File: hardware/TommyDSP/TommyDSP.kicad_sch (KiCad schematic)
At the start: 7 parts

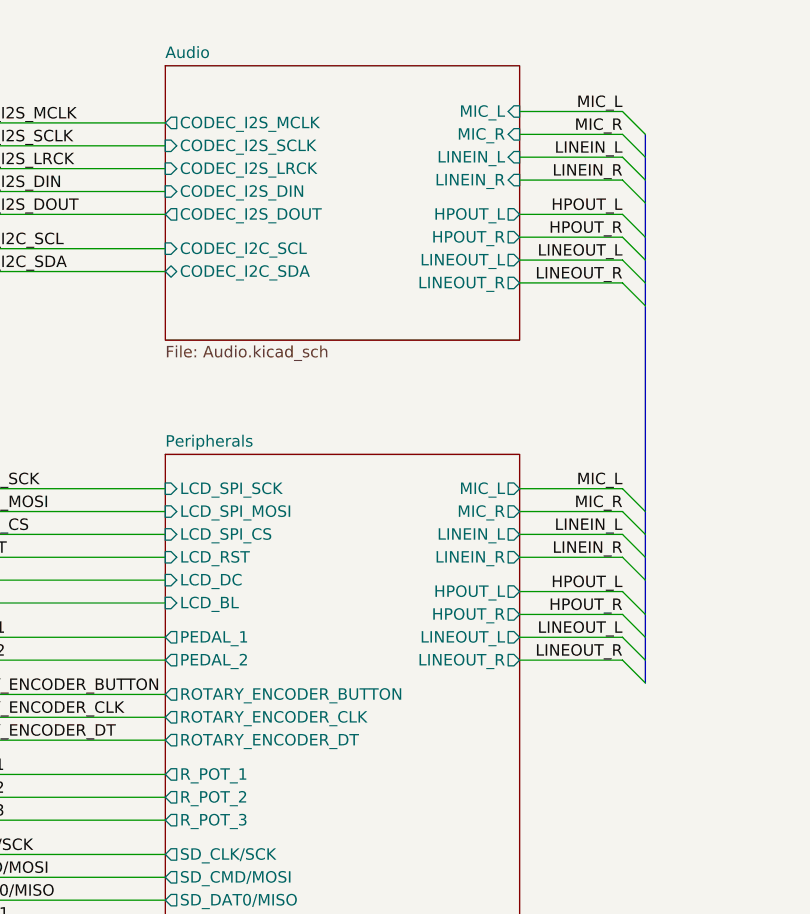
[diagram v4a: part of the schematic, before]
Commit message: hardware: add compatibility for WM8988 CODEC
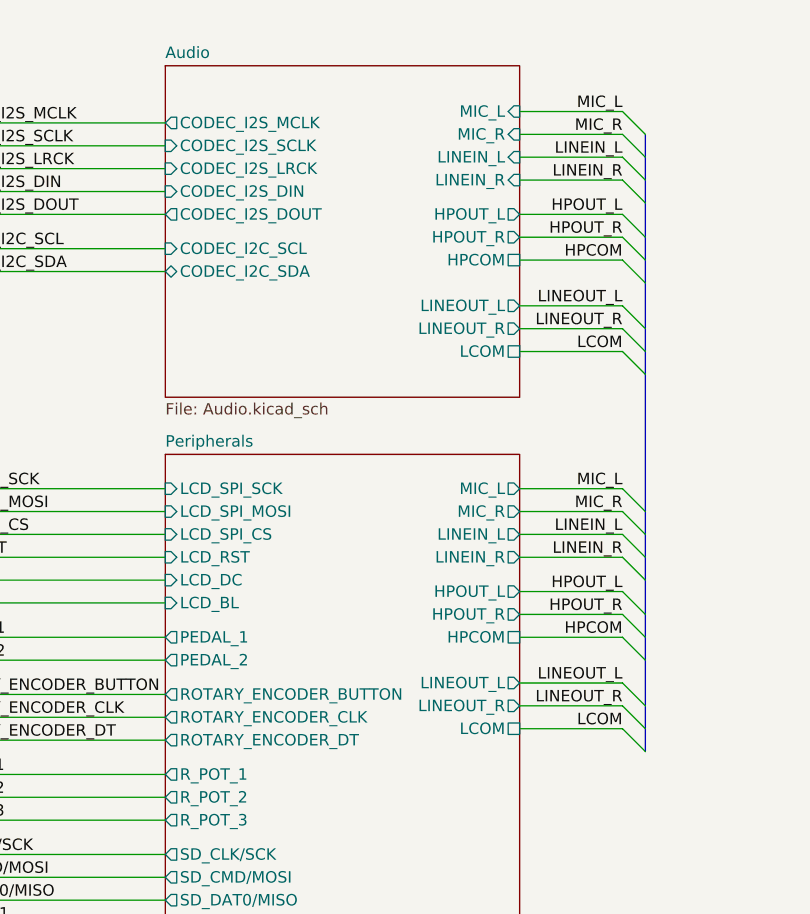
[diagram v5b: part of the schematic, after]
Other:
- sheet Audio ports: added HPCOM, LCOM; removed none
- sheet Peripherals ports: added HPCOM, LCOM; removed none
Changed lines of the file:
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@@
 	)
 	(bus_entry
-		(at 190.5 44.45)
+		(at 190.5 49.53)
 		(size 2.54 2.54)
 		(stroke
@@
 	)
 	(bus_entry
+		(at 190.5 83.82)
+		(size 2.54 2.54)
+		(stroke
+			(width 0)
+			(type default)
+		)
+	)
+	(bus_entry
 		(at 190.5 81.28)
 		(size 2.54 2.54)
@@
 	)
 	(bus_entry
+		(at 190.5 41.91)
+		(size 2.54 2.54)
+		(stroke
+			(width 0)
+			(type default)
+		)
+	)
+	(bus_entry
 		(at 190.5 69.85)
 		(size 2.54 2.54)
@@
 	)
 	(bus_entry
-		(at 190.5 41.91)
+		(at 190.5 93.98)
+		(size 2.54 2.54)
+		(stroke
+			(width 0)
+			(type default)
+		)
+	)
+	(bus_entry
+		(at 190.5 46.99)
 		(size 2.54 2.54)
 		(stroke
@@
 	)
 	(bus_entry
-		(at 190.5 83.82)
+		(at 190.5 88.9)
+		(size 2.54 2.54)
+		(stroke
+			(width 0)
+			(type default)
+		)
+	)
+	(bus_entry
+		(at 190.5 91.44)
 		(size 2.54 2.54)
 		(stroke
@@
 	)
 	(bus_entry
-		(at 190.5 86.36)
+		(at 190.5 52.07)
 		(size 2.54 2.54)
 		(stroke
@@
 		)
 	)
+	(bus
+		(pts
+			(xy 193.04 86.36) (xy 193.04 91.44)
+		)
+		(stroke
+			(width 0)
+			(type default)
+		)
+	)
 	(wire
 		(pts
@@
 	(wire
 		(pts
+			(xy 179.07 52.07) (xy 190.5 52.07)
+		)
+		(stroke
+			(width 0)
+			(type default)
+		)
+	)
+	(wire
+		(pts
 			(xy 114.3 115.57) (xy 139.7 115.57)
 		)
@@
 	(bus
 		(pts
-			(xy 193.04 44.45) (xy 193.04 46.99)
+			(xy 193.04 49.53) (xy 193.04 52.07)
 		)
 		(stroke
@@
 	(wire
 		(pts
+			(xy 179.07 41.91) (xy 190.5 41.91)
+		)
+		(stroke
+			(width 0)
+			(type default)
+		)
+	)
+	(wire
+		(pts
 			(xy 63.5 105.41) (xy 76.2 105.41)
 		)
@@
 	(bus
 		(pts
-			(xy 193.04 86.36) (xy 193.04 88.9)
+			(xy 193.04 91.44) (xy 193.04 93.98)
 		)
 		(stroke
@@
 	(wire
 		(pts
-			(xy 179.07 44.45) (xy 190.5 44.45)
+			(xy 179.07 49.53) (xy 190.5 49.53)
 		)
 		(stroke
@@
 	(wire
 		(pts
-			(xy 179.07 41.91) (xy 190.5 41.91)
+			(xy 179.07 46.99) (xy 190.5 46.99)
 		)
 		(stroke
@@
 	(wire
 		(pts
+			(xy 179.07 93.98) (xy 190.5 93.98)
+		)
+		(stroke
+			(width 0)
+			(type default)
+		)
+	)
+	(wire
+		(pts
 			(xy 63.5 72.39) (xy 88.9 72.39)
 		)
@@
 		)
 	)
+	(bus
+		(pts
+			(xy 193.04 44.45) (xy 193.04 49.53)
+		)
+		(stroke
+			(width 0)
+			(type default)
+		)
+	)
 	(wire
 		(pts
@@
 		)
 	)
+	(bus
+		(pts
+			(xy 193.04 93.98) (xy 193.04 96.52)
+		)
+		(stroke
+			(width 0)
+			(type default)
+		)
+	)
 	(wire
 		(pts
@@
 	(wire
 		(pts
-			(xy 179.07 86.36) (xy 190.5 86.36)
+			(xy 179.07 91.44) (xy 190.5 91.44)
 		)
 		(stroke
@@
 	(bus
 		(pts
-			(xy 193.04 46.99) (xy 193.04 69.85)
+			(xy 193.04 52.07) (xy 193.04 54.61)
 		)
 		(stroke
@@
 	(wire
 		(pts
+			(xy 179.07 83.82) (xy 190.5 83.82)
+		)
+		(stroke
+			(width 0)
+			(type default)
+		)
+	)
+	(wire
+		(pts
 			(xy 179.07 30.48) (xy 190.5 30.48)
 		)
@@
 		)
 	)
+	(bus
+		(pts
+			(xy 193.04 54.61) (xy 193.04 69.85)
+		)
+		(stroke
+			(width 0)
+			(type default)
+		)
+	)
 	(wire
 		(pts
@@
 	(wire
 		(pts
-			(xy 179.07 83.82) (xy 190.5 83.82)
+			(xy 179.07 88.9) (xy 190.5 88.9)
 		)
 		(stroke
@@
 		)
 	)
+	(label "LCOM"
+		(at 190.5 93.98 180)
+		(effects
+			(font
+				(size 1.27 1.27)
+			)
+			(justify right bottom)
+		)
+	)
 	(label "LINEOUT_L"
-		(at 190.5 83.82 180)
+		(at 190.5 88.9 180)
 		(effects
 			(font
@@
 	)
 	(label "LINEOUT_R"
-		(at 190.5 86.36 180)
+		(at 190.5 91.44 180)
 		(effects
 			(font
@@
 	)
 	(label "LINEOUT_R"
-		(at 190.5 44.45 180)
+		(at 190.5 49.53 180)
 		(effects
 			(font
@@
 		)
 	)
+	(label "LCOM"
+		(at 190.5 52.07 180)
+		(effects
+			(font
+				(size 1.27 1.27)
+			)
+			(justify right bottom)
+		)
+	)
+	(label "HPCOM"
+		(at 190.5 83.82 180)
+		(effects
+			(font
+				(size 1.27 1.27)
+			)
+			(justify right bottom)
+		)
+	)
 	(label "CODEC_I2S_DOUT"
 		(at 88.9 34.29 180)
@@
 	)
 	(label "LINEOUT_L"
+		(at 190.5 46.99 180)
+		(effects
+			(font
+				(size 1.27 1.27)
+			)
+			(justify right bottom)
+		)
+	)
+	(label "HPCOM"
 		(at 190.5 41.91 180)
 		(effects
@@
 		)
 		(pin "LINEOUT_L" output
-			(at 179.07 83.82 0)
+			(at 179.07 88.9 0)
 			(effects
 				(font
@@
 		)
 		(pin "LINEOUT_R" output
-			(at 179.07 86.36 0)
+			(at 179.07 91.44 0)
 			(effects
 				(font
@@
 			)
 		)
+		(pin "LCOM" passive
+			(at 179.07 93.98 0)
+			(effects
+				(font
+					(size 1.27 1.27)
+				)
+				(justify right)
+			)
+		)
+		(pin "HPCOM" passive
+			(at 179.07 83.82 0)
+			(effects
+				(font
+					(size 1.27 1.27)
+				)
+				(justify right)
+			)
+		)
 		(instances
 			(project "TommyDSP"
@@
 	(sheet
 		(at 139.7 20.32)
-		(size 39.37 30.48)
+		(size 39.37 36.83)
 		(exclude_from_sim no)
 		(in_bom yes)
@@
 		)
 		(property "Sheetfile" "Audio.kicad_sch"
-			(at 139.7 51.3846 0)
+			(at 139.7 57.7346 0)
 			(effects
 				(font
@@
 		)
 		(pin "LINEOUT_L" output
-			(at 179.07 41.91 0)
+			(at 179.07 46.99 0)
 			(effects
 				(font
@@
 		)
 		(pin "LINEOUT_R" output
-			(at 179.07 44.45 0)
+			(at 179.07 49.53 0)
 			(effects
 				(font
@@
 			(effects
 				(font
+					(size 1.27 1.27)
+				)
+				(justify right)
+			)
+		)
+		(pin "HPCOM" passive
+			(at 179.07 41.91 0)
+			(effects
+				(font
+					(size 1.27 1.27)
+				)
+				(justify right)
+			)
+		)
+		(pin "LCOM" passive
+			(at 179.07 52.07 0)
+			(effects
+				(font
